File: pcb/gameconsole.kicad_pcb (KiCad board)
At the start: 2 copper layers, 61 x 85.9 mm, 5 parts

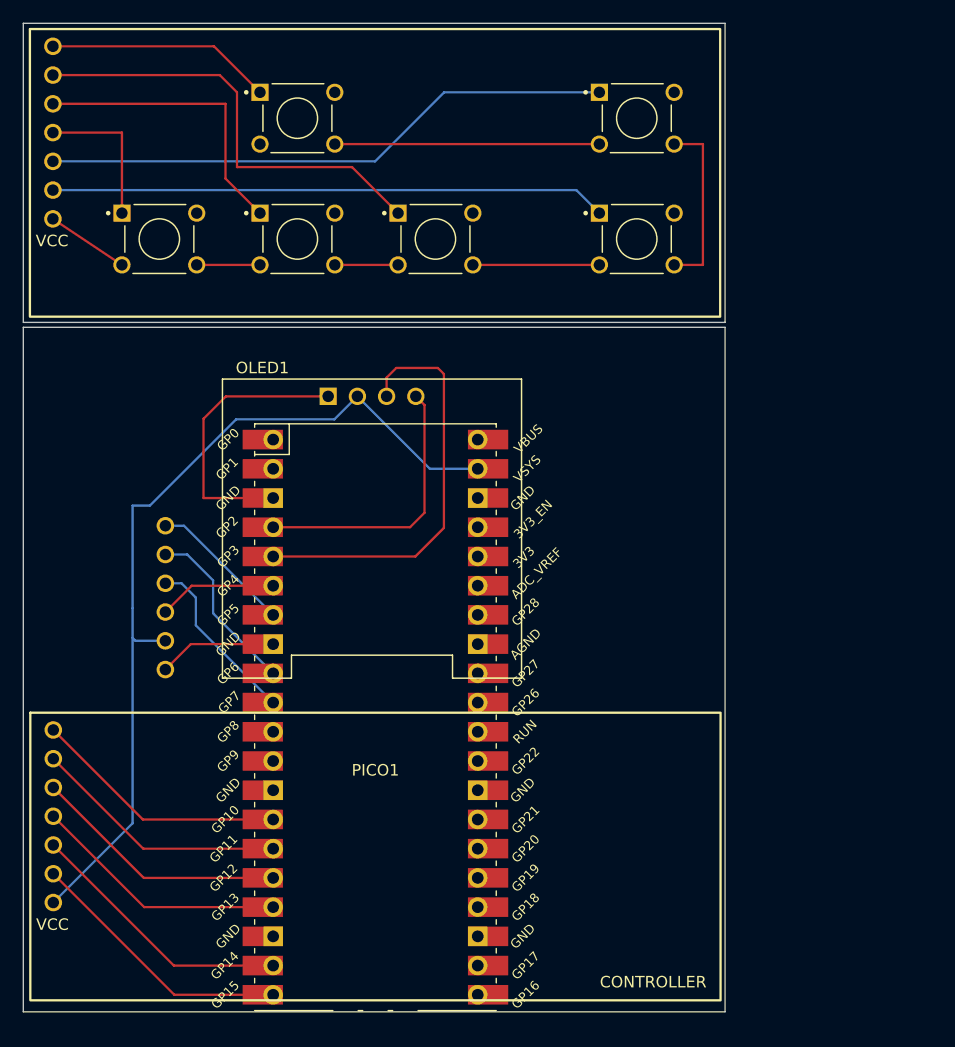
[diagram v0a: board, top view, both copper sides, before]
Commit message: Update PCB files
I redesigned the overall footprint to be slimmer, as well as fixed several critical oversights like a component being upside down.
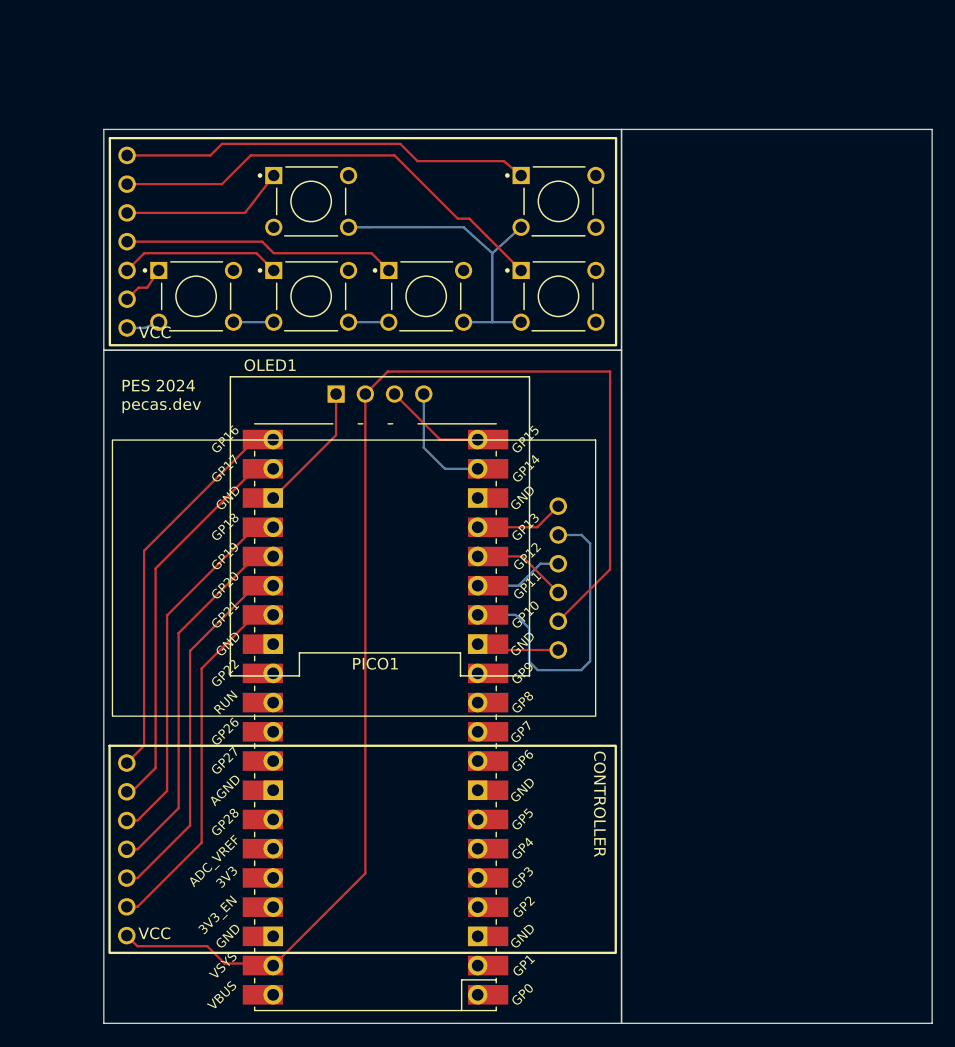
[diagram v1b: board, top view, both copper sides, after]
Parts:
- SDCARD1: moved to F.Cu
- moved SDCARD1 40.7 mm to (148.8, 98.5)
- moved CONTROLLER1 24.8 mm to (106.5, 125.1)
- moved U 11.8 mm to (106.5, 72.3)
- moved OLED1 0.72 mm to (130.0, 106.0)
- turned PICO1 to 180 degrees
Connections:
- CONTROLLER1 pad 1: Net-(CONTROLLER1-UP) -> Net-(CONTROLLER1-BETA)
- CONTROLLER1 pad 2: Net-(CONTROLLER1-RIGHT) -> Net-(CONTROLLER1-ALPHA)
- CONTROLLER1 pad 3: Net-(CONTROLLER1-DOWN) -> Net-(CONTROLLER1-UP)
- CONTROLLER1 pad 4: Net-(CONTROLLER1-LEFT) -> Net-(CONTROLLER1-RIGHT)
- CONTROLLER1 pad 5: Net-(CONTROLLER1-ALPHA) -> Net-(CONTROLLER1-DOWN)
- CONTROLLER1 pad 6: Net-(CONTROLLER1-BETA) -> Net-(CONTROLLER1-LEFT)
- PICO1 pad 10: Net-(PICO1-GPIO7) -> unconnected-(PICO1-GPIO7-Pad10)
- PICO1 pad 13: unconnected-(PICO1-GND-Pad13) -> Net-(SDCARD1-GND)
- PICO1 pad 14: Net-(CONTROLLER1-UP) -> Net-(PICO1-GPIO10)
- PICO1 pad 15: Net-(CONTROLLER1-RIGHT) -> Net-(PICO1-GPIO11)
- PICO1 pad 16: Net-(CONTROLLER1-DOWN) -> Net-(PICO1-GPIO12)
- PICO1 pad 17: Net-(CONTROLLER1-LEFT) -> Net-(PICO1-GPIO13)
- PICO1 pad 19: Net-(CONTROLLER1-ALPHA) -> Net-(OLED1-SDA)
- PICO1 pad 20: Net-(CONTROLLER1-BETA) -> Net-(OLED1-SCL)
- PICO1 pad 21: unconnected-(PICO1-GPIO16-Pad21) -> Net-(CONTROLLER1-BETA)
- PICO1 pad 22: unconnected-(PICO1-GPIO17-Pad22) -> Net-(CONTROLLER1-ALPHA)
- PICO1 pad 23: unconnected-(PICO1-GND-Pad23) -> Net-(OLED1-GND)
- PICO1 pad 24: unconnected-(PICO1-GPIO18-Pad24) -> Net-(CONTROLLER1-UP)
- PICO1 pad 25: unconnected-(PICO1-GPIO19-Pad25) -> Net-(CONTROLLER1-RIGHT)
- PICO1 pad 26: unconnected-(PICO1-GPIO20-Pad26) -> Net-(CONTROLLER1-DOWN)
- PICO1 pad 27: unconnected-(PICO1-GPIO21-Pad27) -> Net-(CONTROLLER1-LEFT)
- PICO1 pad 3: Net-(OLED1-GND) -> unconnected-(PICO1-GND-Pad3)
- PICO1 pad 4: Net-(OLED1-SDA) -> unconnected-(PICO1-GPIO2-Pad4)
- PICO1 pad 5: Net-(OLED1-SCL) -> unconnected-(PICO1-GPIO3-Pad5)
- PICO1 pad 6: Net-(PICO1-GPIO4) -> unconnected-(PICO1-GPIO4-Pad6)
- PICO1 pad 7: Net-(PICO1-GPIO5) -> unconnected-(PICO1-GPIO5-Pad7)
- PICO1 pad 8: Net-(SDCARD1-GND) -> unconnected-(PICO1-GND-Pad8)
- PICO1 pad 9: Net-(PICO1-GPIO6) -> unconnected-(PICO1-GPIO6-Pad9)
- SDCARD1 pad 1: Net-(PICO1-GPIO5) -> Net-(PICO1-GPIO13)
- SDCARD1 pad 2: Net-(PICO1-GPIO6) -> Net-(PICO1-GPIO10)
- SDCARD1 pad 3: Net-(PICO1-GPIO7) -> Net-(PICO1-GPIO11)
- SDCARD1 pad 4: Net-(PICO1-GPIO4) -> Net-(PICO1-GPIO12)
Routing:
- net Net-(CONTROLLER1-VCC): track 76.9 -> 112.5 mm
- net Net-(OLED1-SCL): track 36.4 -> 8.87 mm
- net Net-(PICO1-GPIO10): track 0.00 -> 27.4 mm
- net Net-(PICO1-GPIO6): track 15.3 -> 0.00 mm
- net Net-(PICO1-GPIO7): track 15.1 -> 0.00 mm
- net Net-(OLED1-SDA): track 24.1 -> 10.1 mm
- net Net-(OLED1-GND): track 24.6 -> 11.3 mm
- net Net-(CONTROLLER1-ALPHA): track 23.5 -> 36.2 mm
- net Net-(PICO1-GPIO5): track 12.6 -> 0.00 mm
- net Net-(PICO1-GPIO4): track 11.0 -> 0.00 mm
- net Net-(CONTROLLER1-BETA): track 23.5 -> 34.3 mm
- net Net-(CONTROLLER1-DOWN): track 22.4 -> 32.8 mm
- net Net-(CONTROLLER1-UP): track 22.3 -> 32.2 mm
- net Net-(CONTROLLER1-RIGHT): track 22.3 -> 32.2 mm
- net Net-(CONTROLLER1-LEFT): track 22.4 -> 32.1 mm
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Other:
- board size 61 x 85.9 mm -> 72 x 77.7 mm
- board text added: "PES 2024 pecas.dev"
